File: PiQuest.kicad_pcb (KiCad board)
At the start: 2 copper layers, 80 x 100 mm, 16 parts, among them SW1 SW_Omron_B3FS, SW10 SW_Omron_B3FS, SW2 SW_Omron_B3FS, SW3 SW_Omron_B3FS, SW4 SW_Omron_B3FS, SW5 SW_Omron_B3FS, SW6 SW_Omron_B3FS, SW7 SW_Omron_B3FS, SW8 SW_Omron_B3FS, SW9 SW_Omron_B3FS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

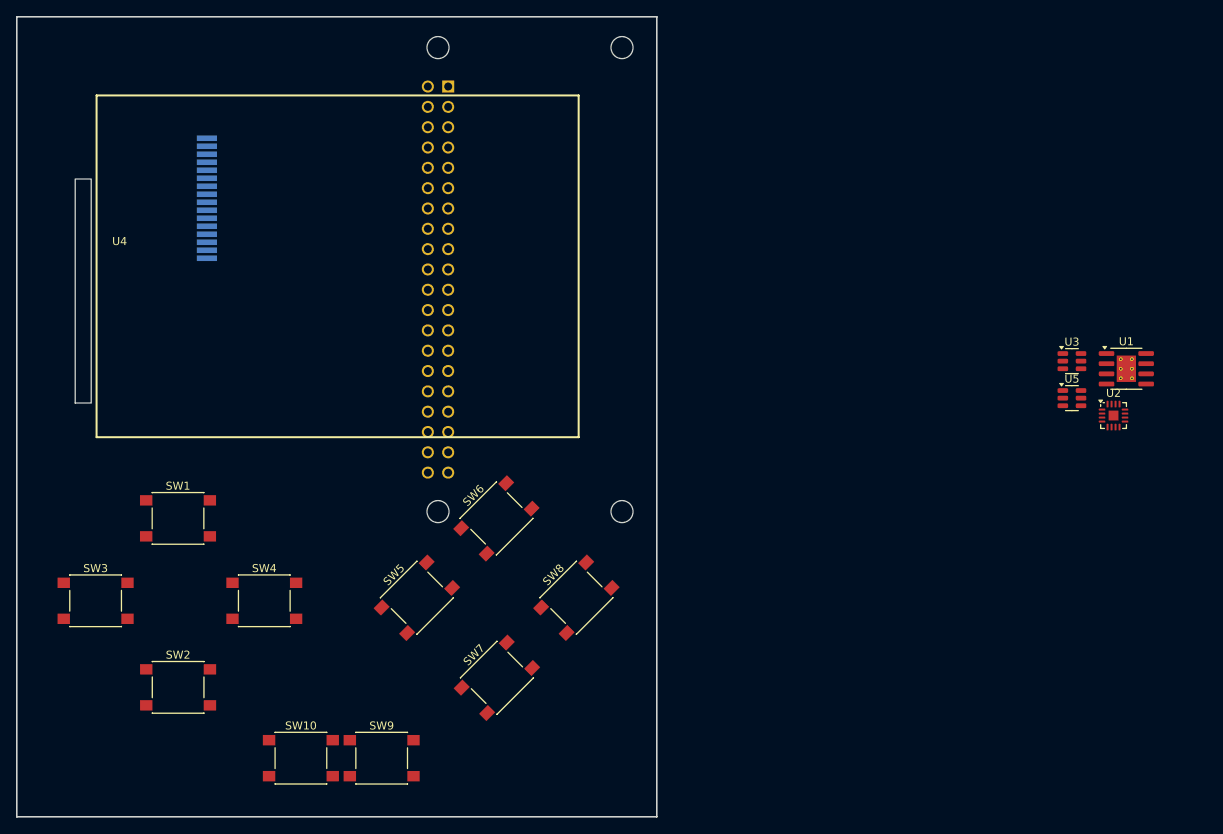
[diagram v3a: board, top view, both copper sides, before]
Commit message: added usb c and fixed alignment issues
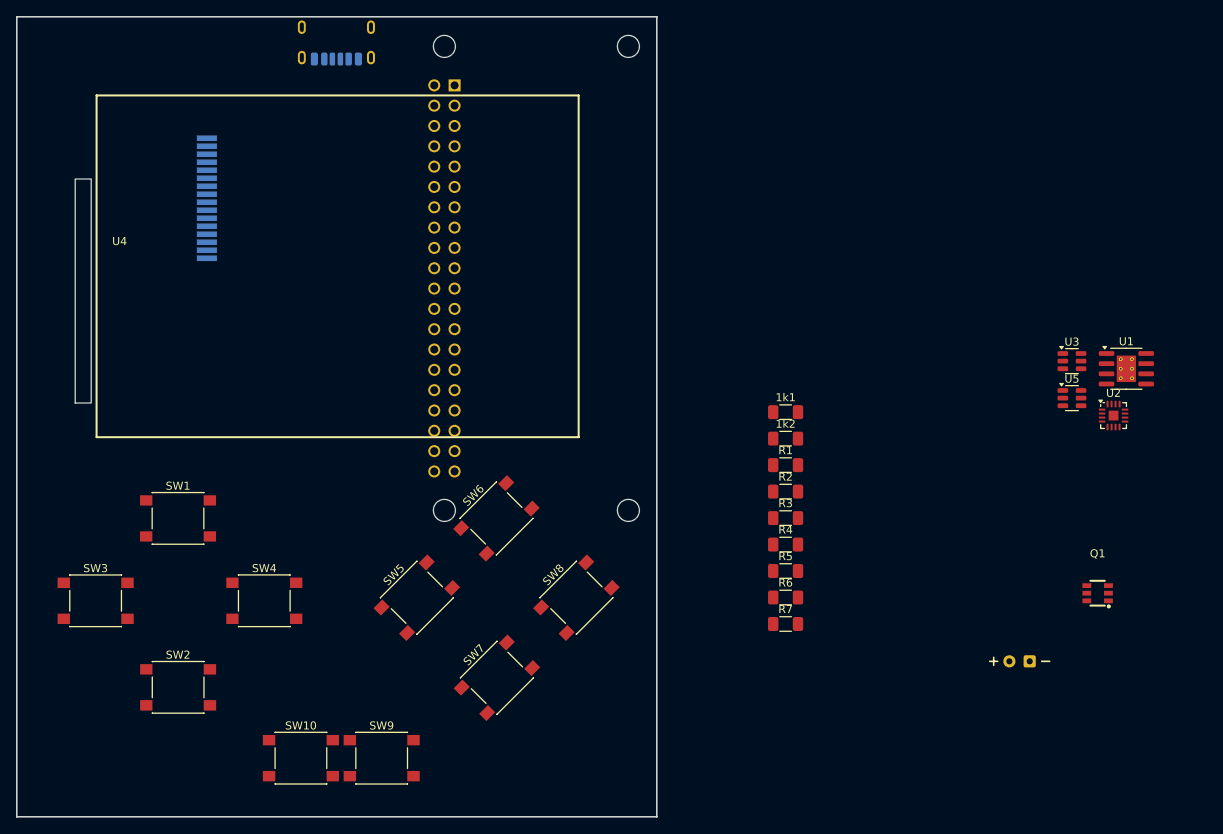
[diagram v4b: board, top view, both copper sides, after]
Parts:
- added 1k1: R, Resistor_SMD:R_1206_3216Metric_Pad1.30x1.75mm_HandSolder, F.Cu at (176.8, 90.6)
- added 1k2: R, Resistor_SMD:R_1206_3216Metric_Pad1.30x1.75mm_HandSolder, F.Cu at (176.8, 93.9)
- added BT1: Battery_Cell, ScottoKeebs_Scotto:Battery, F.Cu at (206.1, 121.8)
- added J2: USB_C_Receptacle_PowerOnly_6P, Connector_USB:USB_C_Receptacle_HRO_TYPE-C-31-M-17, B.Cu at (120.7, 43.3)
- added Q1: FS8205A_C2830320, easyeda2kicad:SOT-23-6_L2.9-W1.6-P0.95-LS2.8-BR, F.Cu at (215.8, 113.2)
- added R1: R, Resistor_SMD:R_1206_3216Metric_Pad1.30x1.75mm_HandSolder, F.Cu at (176.8, 97.2)
- added R2: R, Resistor_SMD:R_1206_3216Metric_Pad1.30x1.75mm_HandSolder, F.Cu at (176.8, 100.5)
- added R3: 100, Resistor_SMD:R_1206_3216Metric_Pad1.30x1.75mm_HandSolder, F.Cu at (176.8, 103.9)
- added R4: 2k, Resistor_SMD:R_1206_3216Metric_Pad1.30x1.75mm_HandSolder, F.Cu at (176.8, 107.2)
- added R5: 2k, Resistor_SMD:R_1206_3216Metric_Pad1.30x1.75mm_HandSolder, F.Cu at (176.8, 110.5)
- added R6: 30k, Resistor_SMD:R_1206_3216Metric_Pad1.30x1.75mm_HandSolder, F.Cu at (176.8, 113.8)
- added R7: 10k, Resistor_SMD:R_1206_3216Metric_Pad1.30x1.75mm_HandSolder, F.Cu at (176.8, 117.1)
- moved A1 0.81 mm to (134.2, 73.9)
